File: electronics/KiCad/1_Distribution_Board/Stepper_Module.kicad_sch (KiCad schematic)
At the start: 17 parts, among them J4 Jumper Pins, J5 Jumper Pins, J6 JST PH, J7 Generic 2.54mm

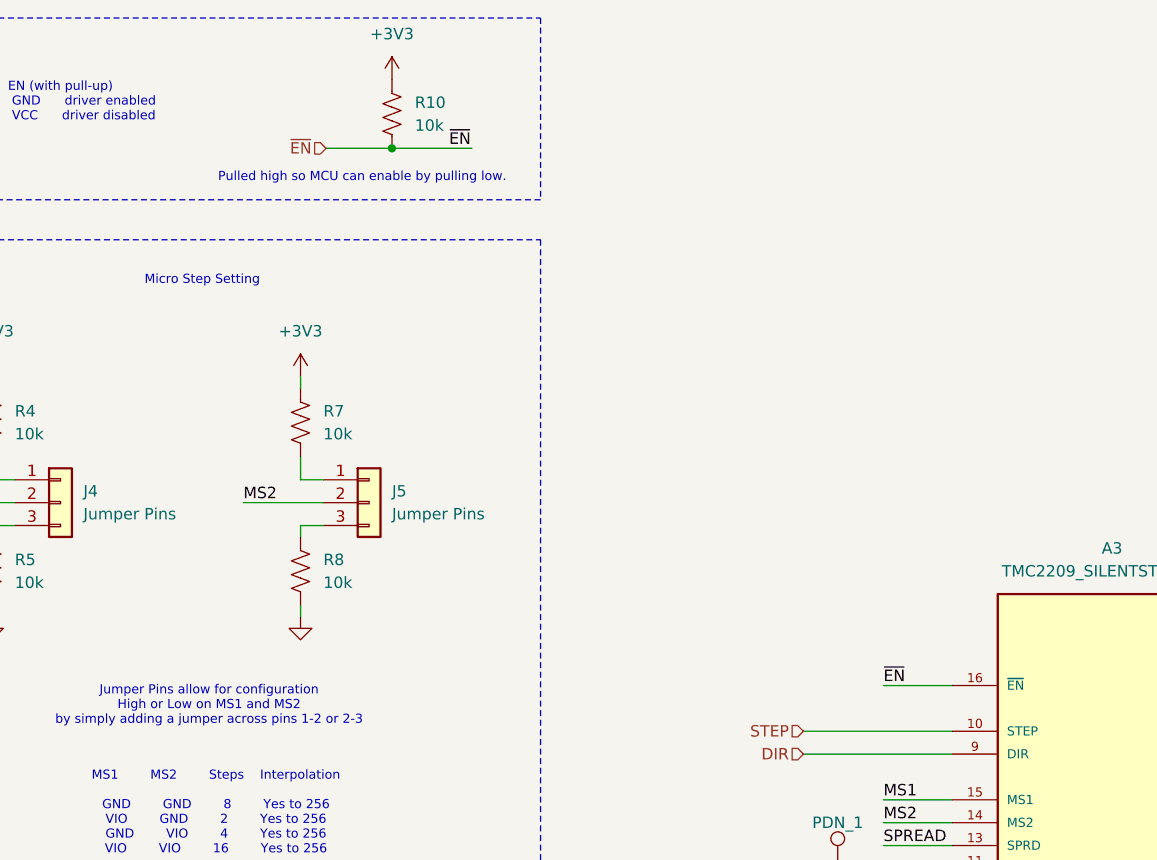
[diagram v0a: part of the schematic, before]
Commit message: Updated Schematic naming, PCB work
Updated Schematic naming for sub-sheets to get rid of untitled and adapter board ones. ADD - 815 sub-sheet for cleaner printable schematic.

PCB:

Started moving modules to socket headers for easy of prototyping.
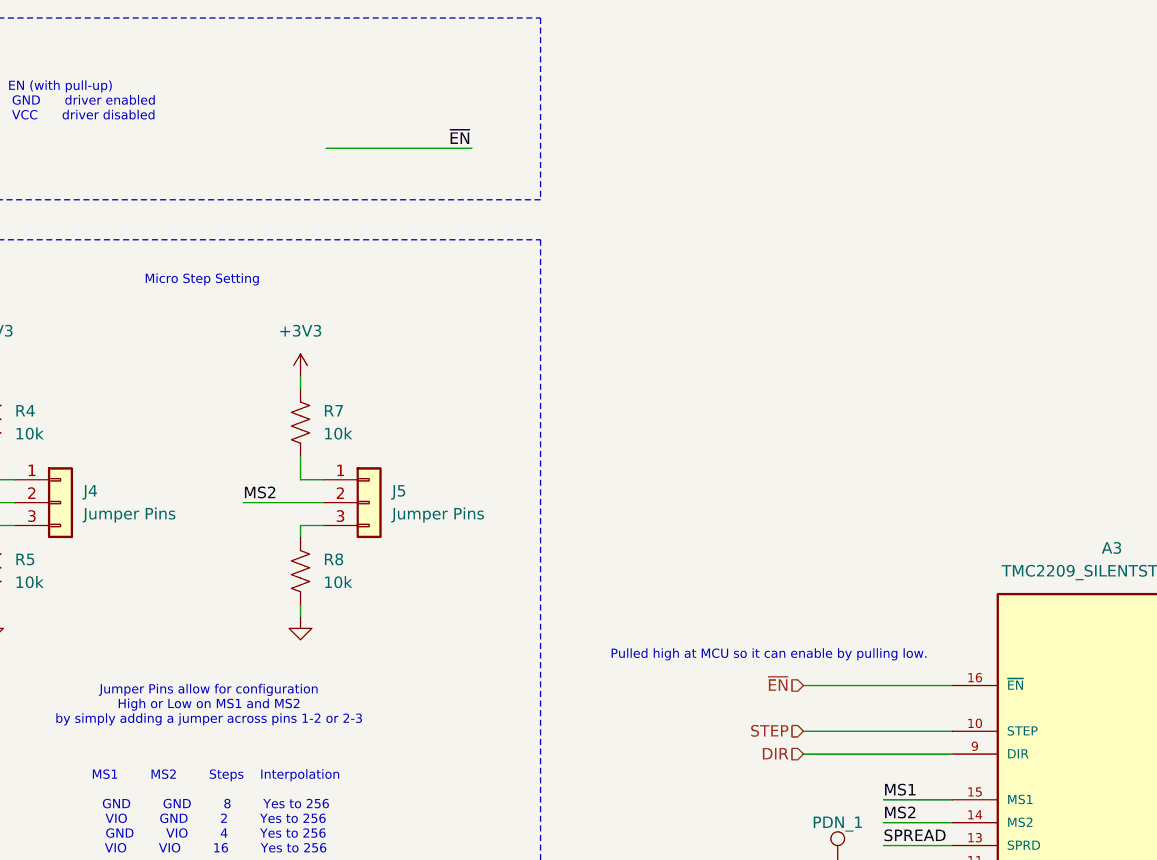
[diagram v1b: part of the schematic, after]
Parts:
- removed R10: 10k, Resistor_SMD:R_0805_2012Metric_Pad1.20x1.40mm_HandSolder, symbol Device:R_US
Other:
- note added: "Pulled high at MCU so it can enable by pulling low."
- note removed: "Pulled high so MCU can enable by pulling low."
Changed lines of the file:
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@@
 	(title_block
 		(title "Distribution Board")
-		(date "2026-01-13")
-		(rev "0.3")
+		(date "2026-01-25")
+		(rev "0.4")
 		(company "basically")
 	)
@@
 		)
 	)
-	(text "Pulled high so MCU can enable by pulling low."
-		(exclude_from_sim no)
-		(at 69.088 33.782 0)
+	(text "Pulled high at MCU so it can enable by pulling low."
+		(exclude_from_sim no)
+		(at 114.3 86.868 0)
 		(effects
 			(font
@@
 	)
 	(junction
-		(at 72.39 30.48)
-		(diameter 0)
-		(color 0 0 0 0)
-	)
-	(junction
 		(at 175.26 71.12)
 		(diameter 0)
@@
 		)
 	)
-	(wire
-		(pts
-			(xy 72.39 30.48) (xy 81.28 30.48)
-		)
-		(stroke
-			(width 0)
-			(type default)
-		)
-	)
 	(polyline
 		(pts
@@
 	(wire
 		(pts
-			(xy 65.0709 30.48) (xy 72.39 30.48)
-		)
-		(stroke
-			(width 0)
-			(type default)
-		)
-	)
-	(wire
-		(pts
-			(xy 127 90.17) (xy 134.62 90.17)
+			(xy 65.0709 30.48) (xy 81.28 30.48)
+		)
+		(stroke
+			(width 0)
+			(type default)
+		)
+	)
+	(wire
+		(pts
+			(xy 118.11 90.17) (xy 134.62 90.17)
 		)
 		(stroke
@@
 	(label "M2B"
 		(at 171.45 105.41 0)
-		(effects
-			(font
-				(size 1.27 1.27)
-			)
-			(justify left bottom)
-		)
-	)
-	(label "~{EN}"
-		(at 127 90.17 0)
 		(effects
 			(font
@@
 	(hierarchical_label "~{EN}"
 		(shape input)
-		(at 65.0709 30.48 180)
+		(at 118.11 90.17 180)
 		(effects
 			(font
@@
 				(path "/d53c8c01-e754-4310-8a73-7d7c95e64cd3/ec0756a4-872d-4fc6-b758-9ad2624703a8"
 					(reference "R34")
-					(unit 1)
-				)
-			)
-		)
-	)
-	(symbol
-		(lib_id "power:+3V3")
-		(at 72.39 22.86 0)
-		(unit 1)
-		(exclude_from_sim no)
-		(in_bom yes)
-		(on_board yes)
-		(dnp no)
-		(fields_autoplaced yes)
-		(property "Reference" "#PWR018"
-			(at 72.39 26.67 0)
-			(effects
-				(font
-					(size 1.27 1.27)
-				)
-				(hide yes)
-			)
-		)
-		(property "Value" "+3V3"
-			(at 72.39 17.78 0)
-			(effects
-				(font
-					(size 1.27 1.27)
-				)
-			)
-		)
-		(property "Footprint" ""
-			(at 72.39 22.86 0)
-			(effects
-				(font
-					(size 1.27 1.27)
-				)
-				(hide yes)
-			)
-		)
-		(property "Datasheet" ""
-			(at 72.39 22.86 0)
-			(effects
-				(font
-					(size 1.27 1.27)
-				)
-				(hide yes)
-			)
-		)
-		(property "Description" "Power symbol creates a global label with name \"+3V3\""
-			(at 72.39 22.86 0)
-			(effects
-				(font
-					(size 1.27 1.27)
-				)
-				(hide yes)
-			)
-		)
-		(pin "1"
-		)
-		(instances
-			(project "1_Distribution_Board"
-				(path "/d53c8c01-e754-4310-8a73-7d7c95e64cd3/02dc68e7-469d-4169-b9e6-1742ced64b14"
-					(reference "#PWR018")
-					(unit 1)
-				)
-				(path "/d53c8c01-e754-4310-8a73-7d7c95e64cd3/7a480abb-9b9a-47ac-a44b-24d5185d46e0"
-					(reference "#PWR078")
-					(unit 1)
-				)
-				(path "/d53c8c01-e754-4310-8a73-7d7c95e64cd3/be0591dd-6b80-4d9a-a31b-18ff19c250bb"
-					(reference "#PWR0102")
-					(unit 1)
-				)
-				(path "/d53c8c01-e754-4310-8a73-7d7c95e64cd3/ec0756a4-872d-4fc6-b758-9ad2624703a8"
-					(reference "#PWR090")
 					(unit 1)
 				)
@@
 					(unit 1)
 				)
-			)
-		)
-	)
-	(symbol
-		(lib_id "Device:R_US")
-		(at 72.39 26.67 0)
-		(unit 1)
-		(exclude_from_sim no)
-		(in_bom yes)
-		(on_board yes)
-		(dnp no)
-		(fields_autoplaced yes)
-		(property "Reference" "R10"
-			(at 74.93 25.3999 0)
-			(effects
-				(font
-					(size 1.27 1.27)
-				)
-				(justify left)
-			)
-		)
-		(property "Value" "10k"
-			(at 74.93 27.9399 0)
-			(effects
-				(font
-					(size 1.27 1.27)
-				)
-				(justify left)
-			)
-		)
-		(property "Footprint" "Resistor_SMD:R_0805_2012Metric_Pad1.20x1.40mm_HandSolder"
-			(at 73.406 26.924 90)
-			(effects
-				(font
-					(size 1.27 1.27)
-				)
-				(hide yes)
-			)
-		)
-		(property "Datasheet" "~"
-			(at 72.39 26.67 0)
-			(effects
-				(font
-					(size 1.27 1.27)
-				)
-				(hide yes)
-			)
-		)
-		(property "Description" "Resistor, US symbol"
-			(at 72.39 26.67 0)
-			(effects
-				(font
-					(size 1.27 1.27)
-				)
-				(hide yes)
-			)
-		)
-		(pin "2"
-		)
-		(pin "1"
-		)
-		(instances
-			(project "1_Distribution_Board"
-				(path "/d53c8c01-e754-4310-8a73-7d7c95e64cd3/02dc68e7-469d-4169-b9e6-1742ced64b14"
-					(reference "R10")
-					(unit 1)
-				)
-				(path "/d53c8c01-e754-4310-8a73-7d7c95e64cd3/7a480abb-9b9a-47ac-a44b-24d5185d46e0"
-					(reference "R31")
-					(unit 1)
-				)
-				(path "/d53c8c01-e754-4310-8a73-7d7c95e64cd3/be0591dd-6b80-4d9a-a31b-18ff19c250bb"
-					(reference "R49")
-					(unit 1)
-				)
-				(path "/d53c8c01-e754-4310-8a73-7d7c95e64cd3/ec0756a4-872d-4fc6-b758-9ad2624703a8"
-					(reference "R40")
-					(unit 1)
-				)

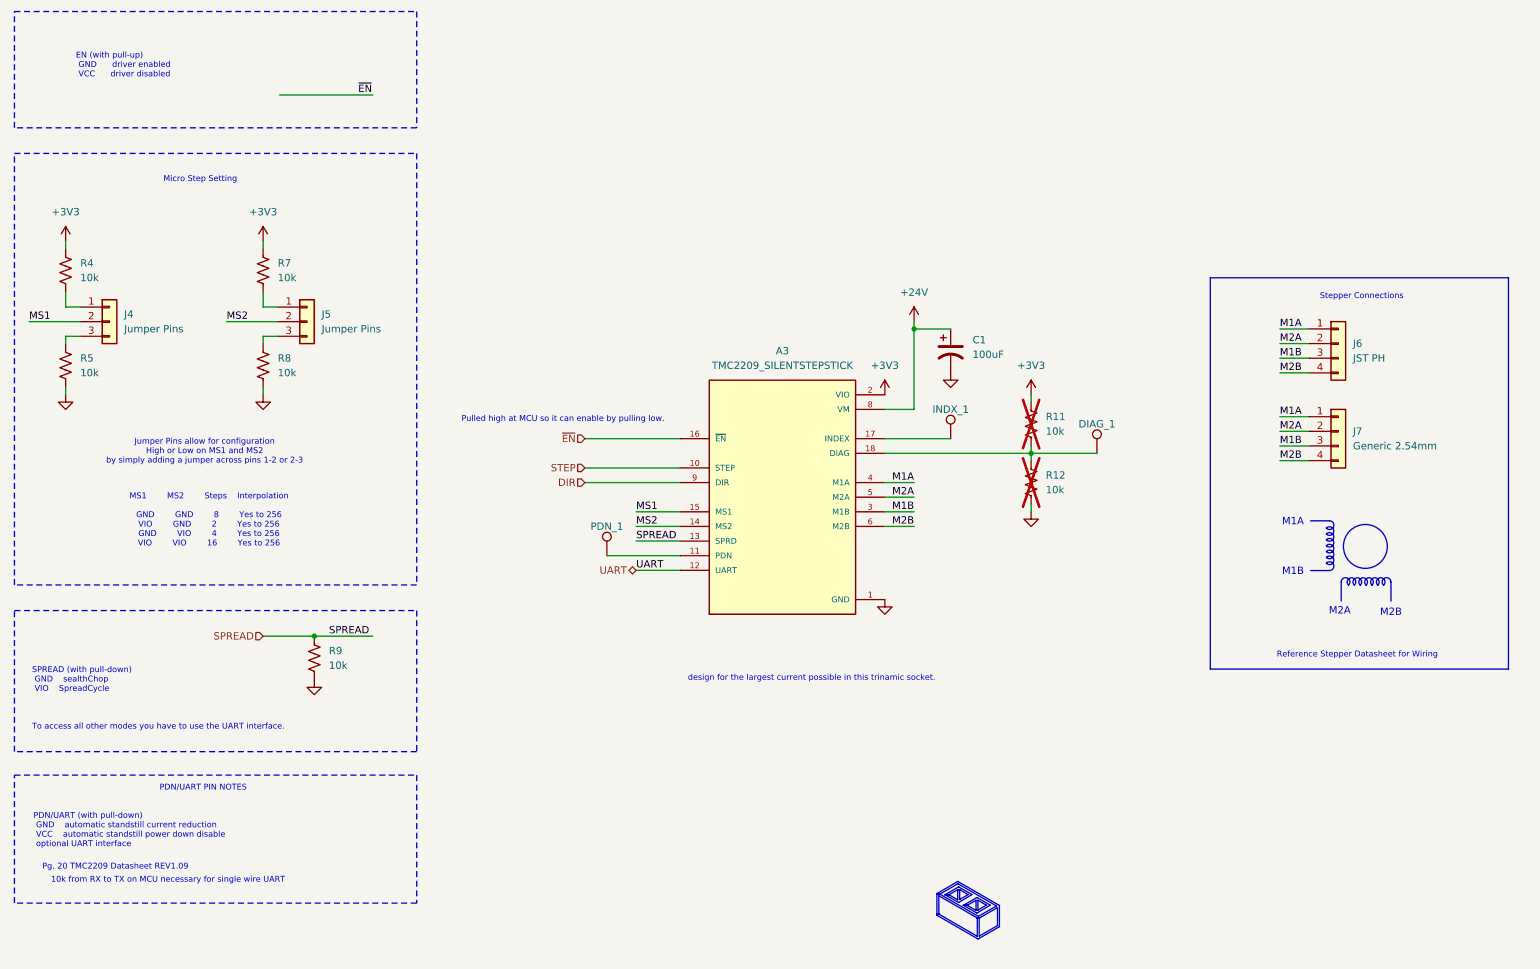
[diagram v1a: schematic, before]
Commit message: PCB updates
Added stepper module headers and working on silk for ease of debug.
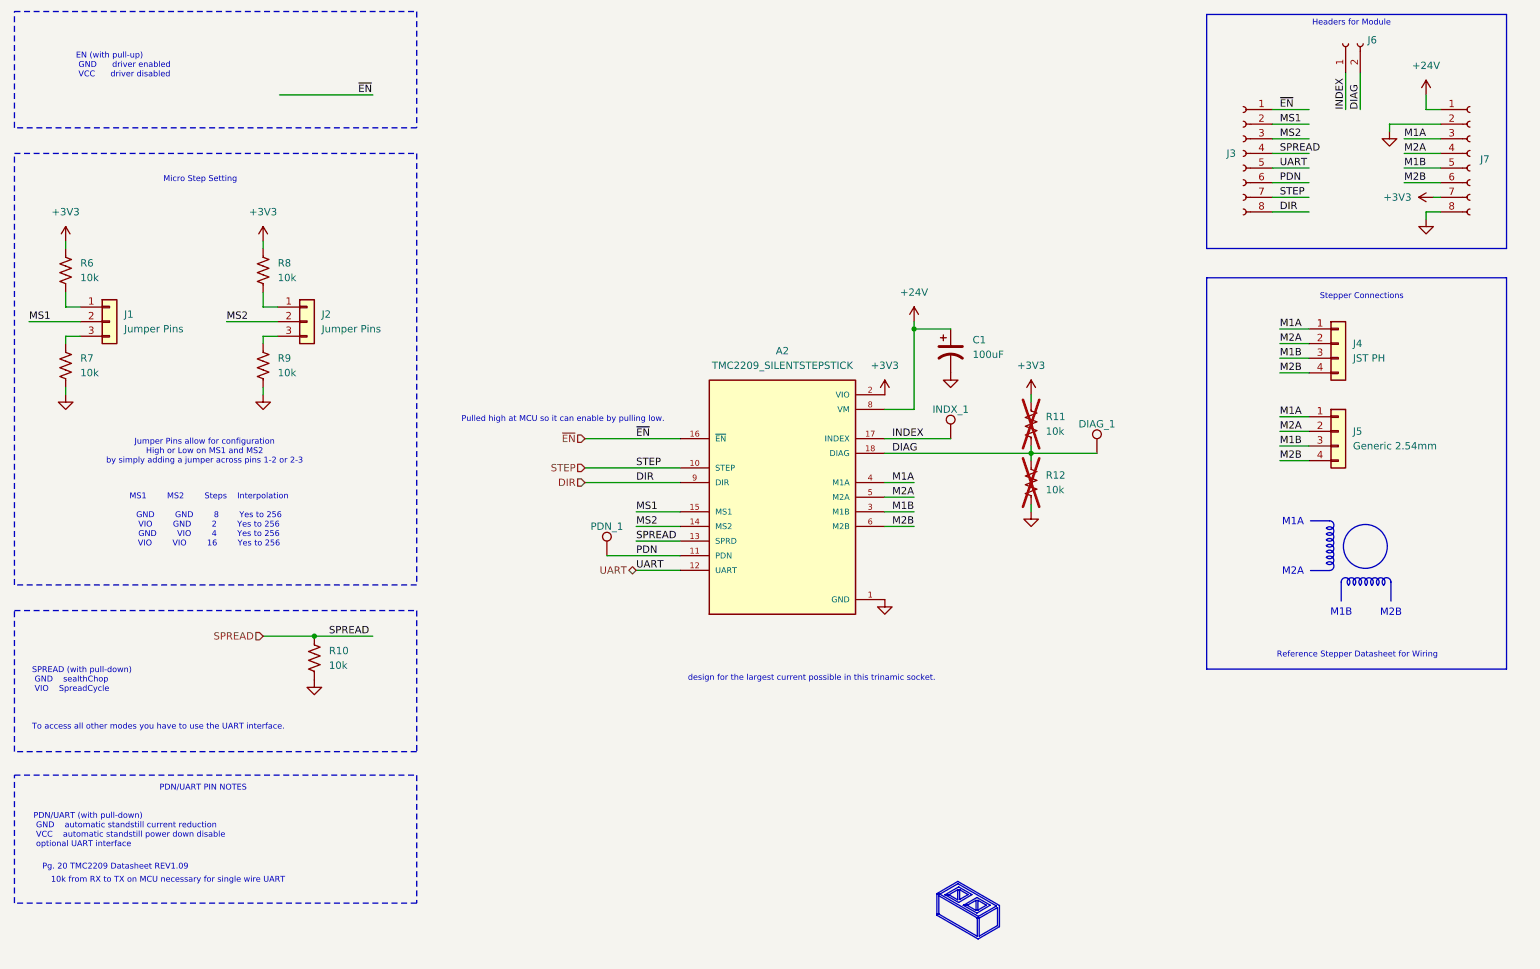
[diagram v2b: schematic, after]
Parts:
- added J3, J7: Conn_01x08_Socket, Connector_PinSocket_2.54mm:PinSocket_1x08_P2.54mm_Vertical, symbol Connector:Conn_01x08_Socket
- added J6: Conn_01x02_Socket, Connector_PinSocket_2.54mm:PinSocket_1x02_P2.54mm_Vertical, symbol Connector:Conn_01x02_Socket
- renumbered A3 to A2, J4 to J1, J5 to J2, J6 to J4, J7 to J5, R9 to R10, R4 to R6, R5 to R7, R7 to R8, R8 to R9
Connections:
- net +24V: now also J7.1 (Pin_1)
- net +3V3: now also J7.7 (Pin_7)
- net DIR: now also J3.8 (Pin_8)
- net GND: now also J7.2 (Pin_2), J7.8 (Pin_8)
- net M1A: now also J7.3 (Pin_3)
- net M1B: now also J7.5 (Pin_5)
- net M2A: now also J7.4 (Pin_4)
- net M2B: now also J7.6 (Pin_6)
- net MS1: now also J3.2 (Pin_2)
- net MS2: now also J3.3 (Pin_3)
- net SPREAD: now also J3.4 (Pin_4)
- net STEP: now also J3.7 (Pin_7)
- net UART: now also J3.5 (Pin_5)
- net ~{EN}: now also J3.1 (Pin_1)
- net INDEX: now reaches A2.17 (INDEX), INDX_1.1
- net INDEX: now also J6.1 (Pin_1)
- net DIAG: now reaches A2.18 (DIAG), DIAG_1.1, R11.2, R12.1
- net DIAG: now also J6.2 (Pin_2)
- net PDN: now reaches A2.11 (PDN), PDN_1.1
- net PDN: now also J3.6 (Pin_6)
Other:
- note added: "Headers for Module"

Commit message: Updated PCB/SCH
Updated stepper schematics and motor schematics for clarity. Updated motor module to use headers. Updated stepper driver top be the BIGTREETECH V1.3. Cleaned up layout locations a bit.
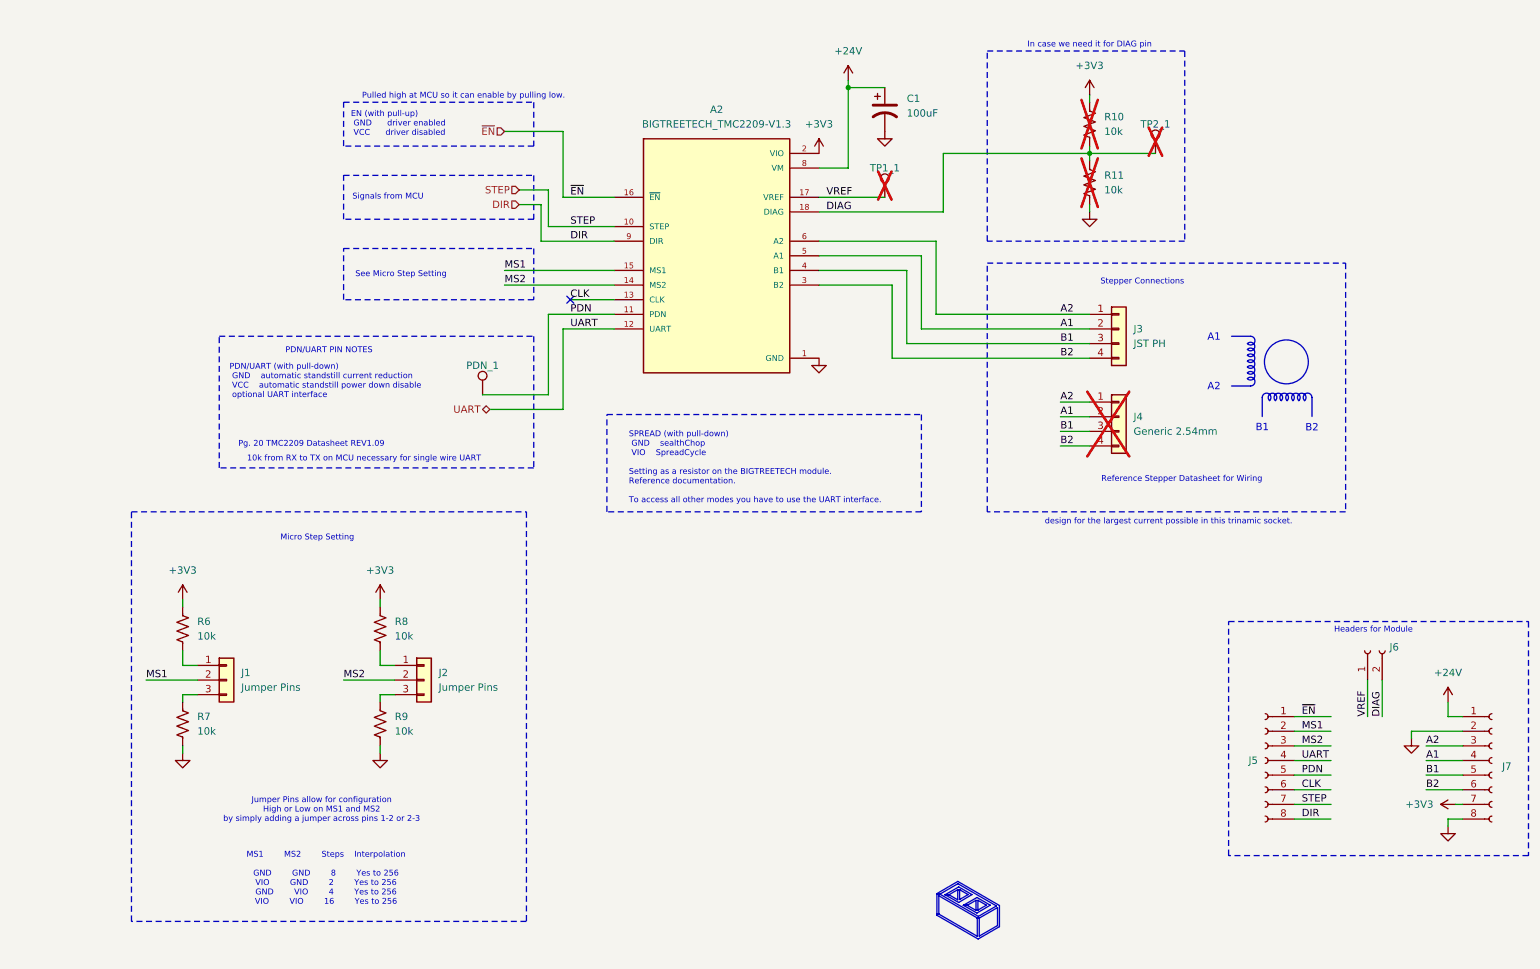
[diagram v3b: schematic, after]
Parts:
- removed A2: TMC2209_SILENTSTEPSTICK, TMC2209_SILENTSTEPSTICK:MODULE_TMC2209_SILENTSTEPSTICK, symbol TMC2209_SILENTSTEPSTICK:TMC2209_SILENTSTEPSTICK
- removed R10: 10k, Resistor_SMD:R_0805_2012Metric_Pad1.20x1.40mm_HandSolder, symbol Device:R_US
- added A2: BIGTREETECH_TMC2209-V1.3, TMC2209_SILENTSTEPSTICK:MODULE_TMC2209_SILENTSTEPSTICK, symbol TMC2209_SILENTSTEPSTICK:BIGTREETECH_TMC2209-V1.3
- J4: renamed from J5; now not fitted
- TP1_1: renamed from INDX_1; now not fitted
- TP2_1: renamed from DIAG_1; now not fitted
- renumbered J4 to J3, J3 to J5, R11 to R10, R12 to R11
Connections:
- net SPREAD is gone; now on net UART: J5.4 (Pin_4)
- net +24V: now also A2.8 (VM)
- net +3V3: now also A2.2 (VIO)
- net DIAG: now also A2.18 (DIAG)
- net DIR: now also A2.9 (DIR)
- net GND: now also A2.1 (GND), A2.7 (GND)
- net MS1: now also A2.15 (MS1)
- net MS2: now also A2.14 (MS2)
- net PDN: now also J5.5 (Pin_5), A2.11 (PDN); no longer J5.6 (Pin_6)
- net STEP: now also A2.10 (STEP)
- net UART: now also A2.12 (UART); no longer J5.5 (Pin_5)
- net ~{EN}: now also A2.16 (~{EN})
- net INDEX renamed VREF
- net VREF: now also A2.17 (VREF)
- net M1A renamed A2
- net A2: now also A2.6 (A2)
- net M1B renamed B1
- net B1: now also A2.4 (B1)
- net M2A renamed A1
- net A1: now also A2.5 (A1)
- net M2B renamed B2
- net B2: now also A2.3 (B2)
- new net CLK: A2.13 (CLK), J5.6 (Pin_6)
- no-connect marks 0 -> 1
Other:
- note added: "A1"
- note added: "A2"
- note added: "B1"
- note added: "B2"
- note added: "In case we need it for DIAG pin"
- note added: "SPREAD (with pull-down) GND sealthChop VIO SpreadCycle Setting as a resistor on the BIGTREETECH module. Reference documentation. To access all other modes you have to use the UART interface."
- note added: "See Micro Step Setting"
- note added: "Signals from MCU"
- note removed: "M1A"
- note removed: "M1B"
- note removed: "M2A"
- note removed: "M2B"
- note removed: "SPREAD (with pull-down) GND sealthChop VIO SpreadCycle To access all other modes you have to use the UART interface."
- moved on the sheet: C1, J1, J2, J3, J5, J6, J7, PDN_1, R10, R11, R6, R7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
